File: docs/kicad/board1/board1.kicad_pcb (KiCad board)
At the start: 2 copper layers, 98 x 98 mm, 37 parts, among them J1 12V_IN, J2 5V_JUMP, J3 MINI_BOX, J4 MECH_THERM, J5 EXT_LED, J6 LCD, J7 TEMP1, J8 TEMP2, M1 BUCK01, M2 SD_TYP0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

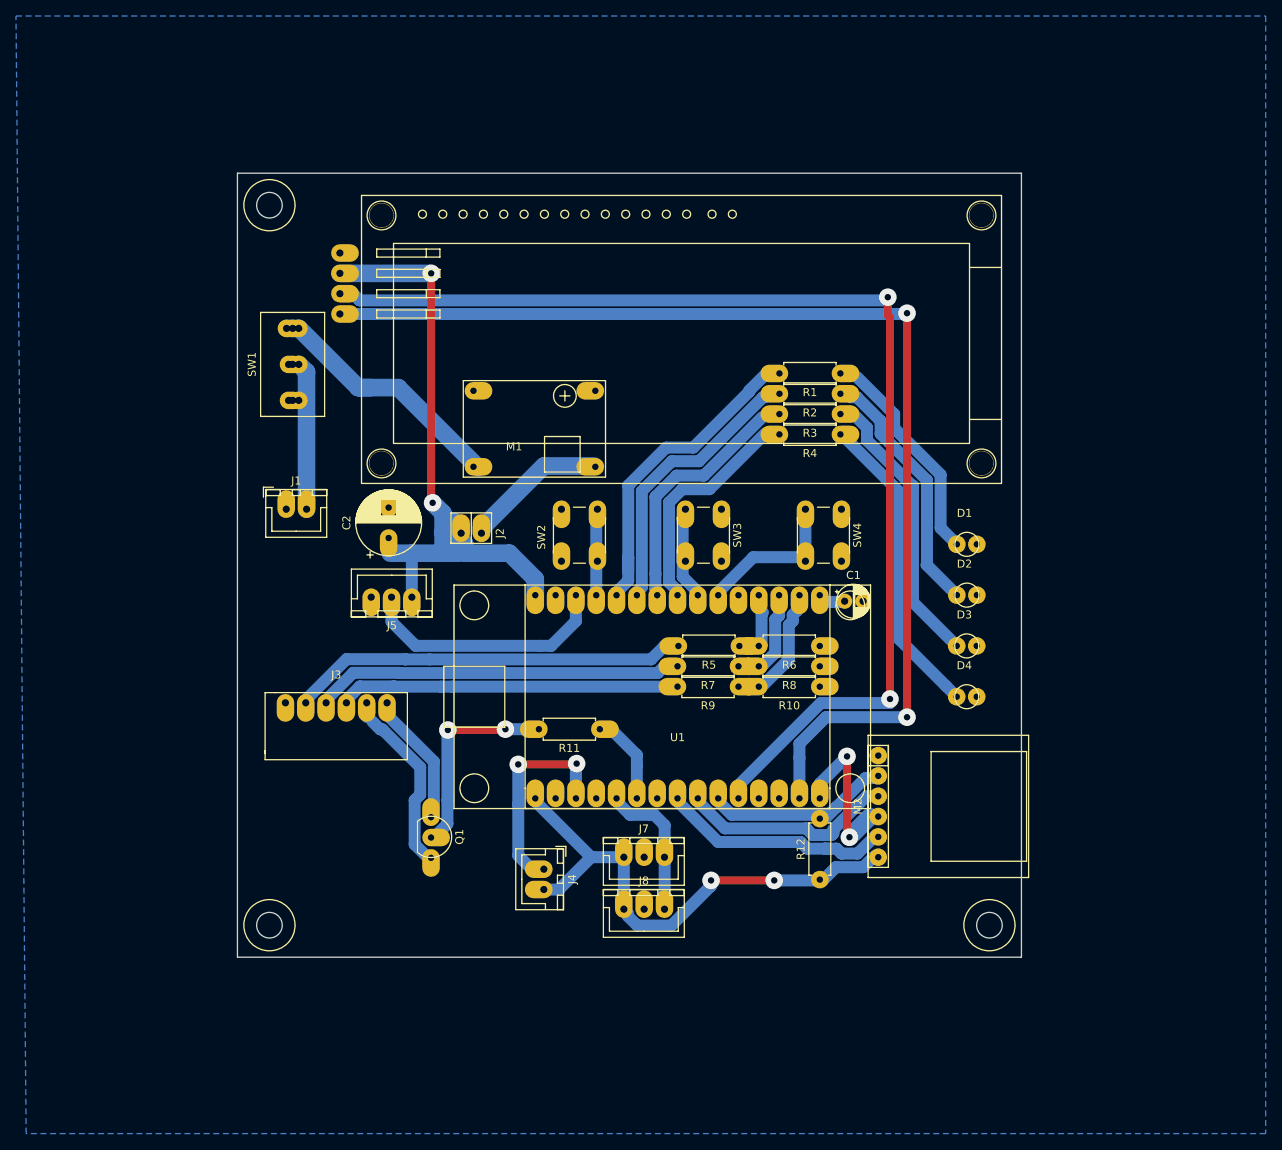
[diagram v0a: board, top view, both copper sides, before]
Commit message: produced fridgeController pcb's "board1" and "miniBox"
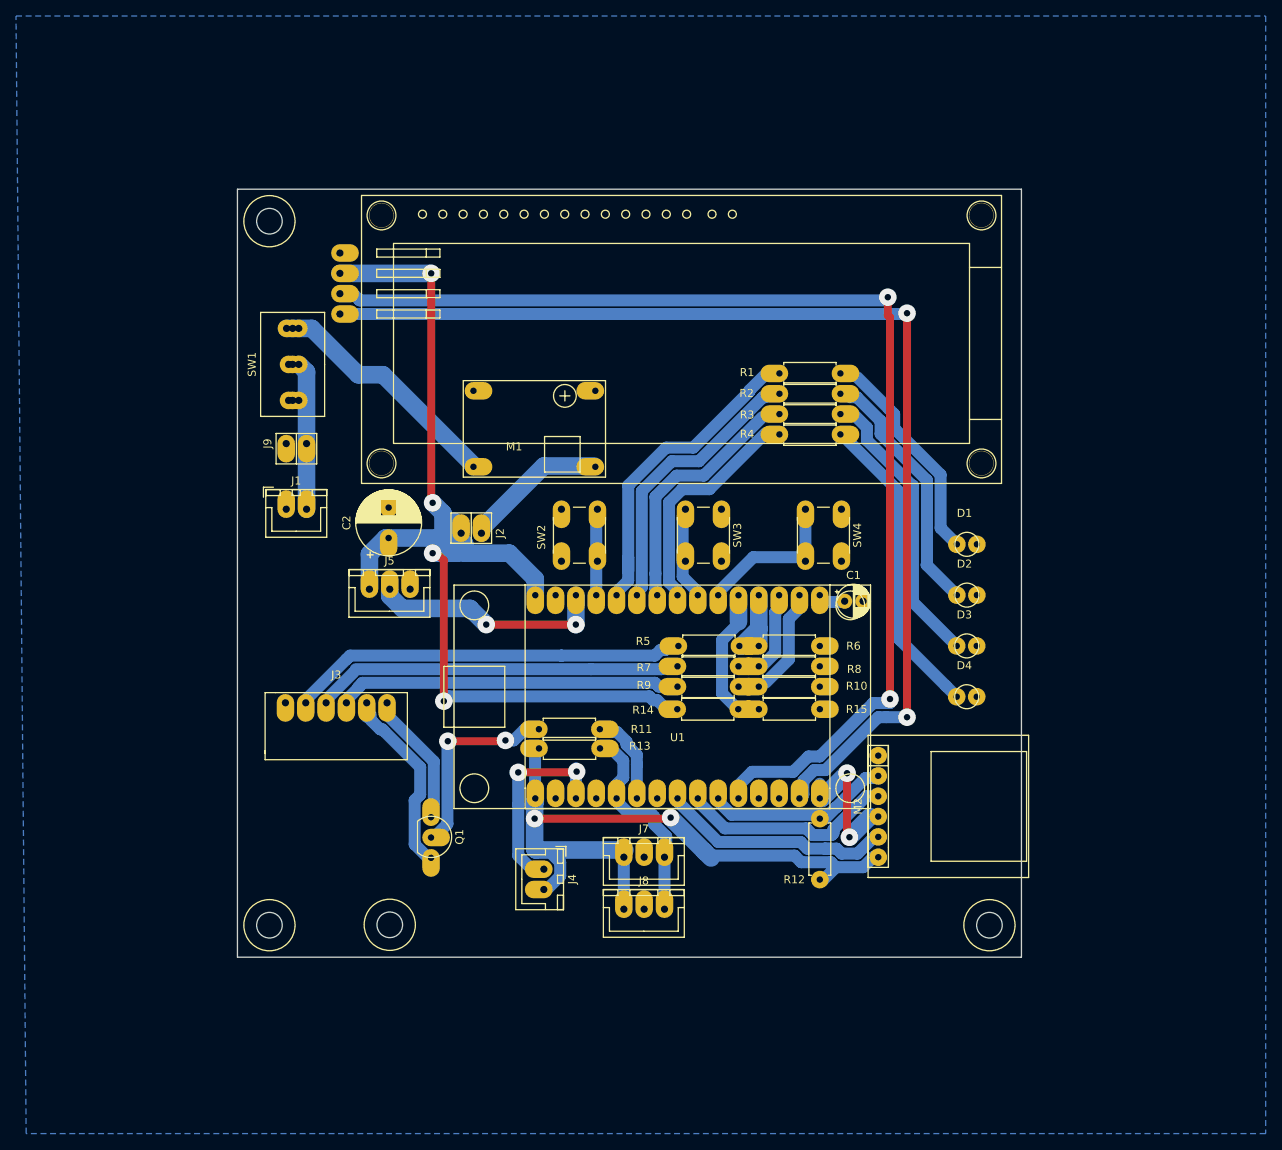
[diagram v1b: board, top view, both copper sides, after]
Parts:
- added J9: 12V_TEST, 0_my_footprints2:pinHeader1x2, F.Cu at (54.1, 59.8)
- added R13: 4.7K, 0_my_footprints2:resistor, F.Cu at (85.7, 97.9)
- added R14: 10K, 0_my_footprints2:resistor, F.Cu at (110.6, 93.0)
- added R15: 4.7K, 0_my_footprints2:resistor, F.Cu at (120.8, 93.0)
- added REF**: myMountingHole_3.2mm_M3, 0_my_footprints:myMountingHole_3.2mm_M3, F.Cu at (67.0, 120.0)
- moved J5 5.39 mm to (64.5, 78.0), turned to 0 degrees
- moved REF** 2.00 mm to (52.0, 32.0)
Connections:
- net C2 renamed C
- U1 pad 11: Net-(U1-Pad11) -> S_5V
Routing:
- net +5V: track 79.6 -> 134.4 mm, vias 2 -> 4
- net +3V3: track 65.6 -> 88.2 mm
- net S_5V: track 0.00 -> 19.2 mm
- net ONE_WIRE: track 18.2 -> 23.7 mm
- net S_PLUS: track 4.55 -> 9.45 mm
- net EXT_LED: track 33.1 -> 29.3 mm, vias 0 -> 2
- net SCL: track 143.1 -> 140.1 mm
- net Net-(Q1-Pad2): track 28.0 -> 25.3 mm
- net MOSI: track 21.6 -> 19.3 mm
- net Net-(M1-Pad4): track 32.8 -> 30.6 mm
- net C: track 22.8 -> 23.8 mm
- net S_FAN: track 9.76 -> 10.5 mm
- net DIAG_DIODE: track 41.9 -> 42.5 mm
- net FAN-: track 45.0 -> 44.5 mm
- net MECH_THERM: track 24.4 -> 23.9 mm
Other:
- board size 98 x 98 mm -> 98 x 96 mm

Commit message: minor changes before more testing ArduinoIDE2.3.3 and Esp32Core3.0.4 on LENOVO-T490-2
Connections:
- J9 pad 2: Net-(J1-Pad2) -> Net-(J9-Pad2)
- SW1 pad 1: Net-(M1-Pad4) -> Net-(SW1-Pad1)
- SW1 pad 2: Net-(J1-Pad2) -> Net-(M1-Pad4)
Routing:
- net Net-(J1-Pad2): track 18.5 -> 14.3 mm
- net Net-(M1-Pad4): track 30.6 -> 28.5 mm

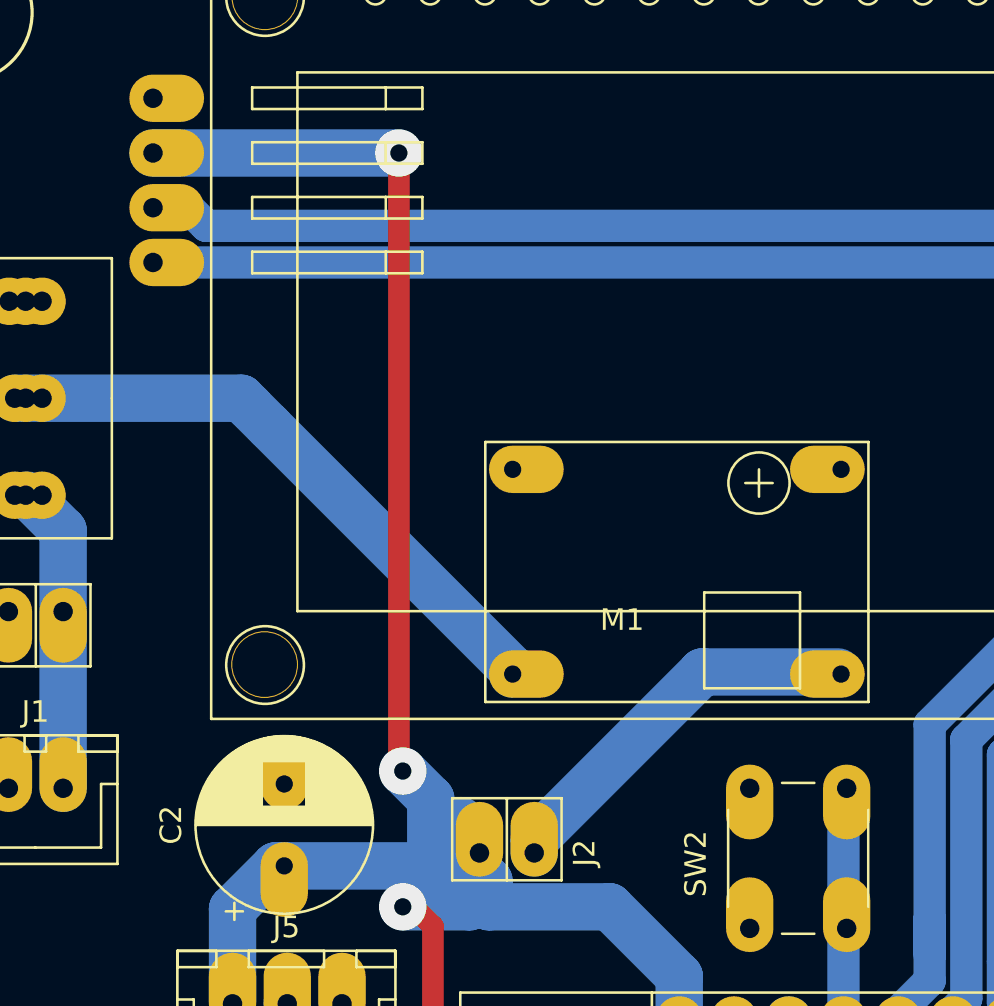
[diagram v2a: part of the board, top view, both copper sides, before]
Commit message: kicad - board1 - rerouted 5V to LCD;  added backflow prevention diode to 5V jumper
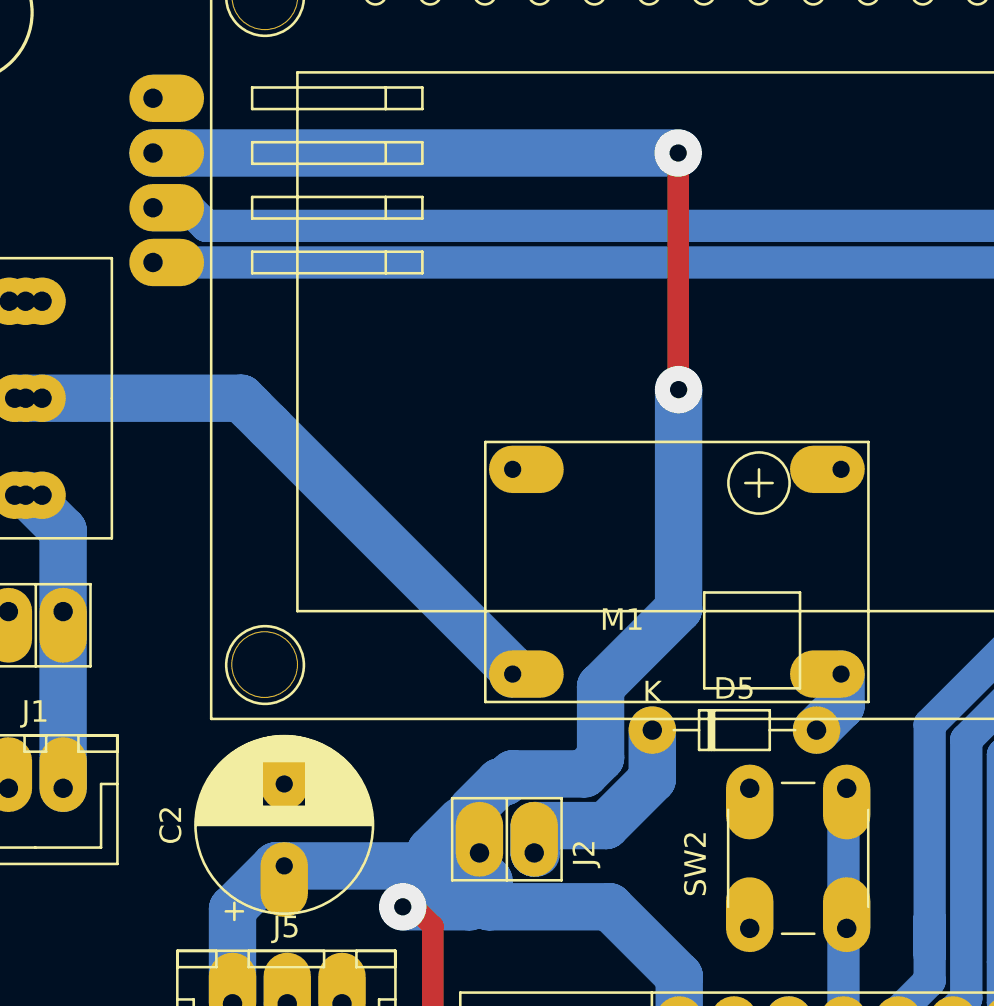
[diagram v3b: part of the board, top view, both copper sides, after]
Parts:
- added D5: 1N4003, 0_my_footprints:myZenerDiode, F.Cu at (84.0, 65.3)
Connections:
- J2 pad 1: Net-(J2-Pad1) -> Net-(D5-Pad1)
- M1 pad 3: Net-(J2-Pad1) -> Net-(D5-Pad2)
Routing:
- net Net-(J2-Pad1): track 17.9 -> 0.00 mm
- net +5V: track 134.4 -> 150.9 mm
- net Net-(D5-Pad1): track 0.00 -> 11.8 mm
- net Net-(D5-Pad2): track 0.00 -> 3.07 mm
